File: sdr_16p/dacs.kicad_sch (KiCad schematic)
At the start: 1 part, among them U5 ADAU1962AWBSTZ

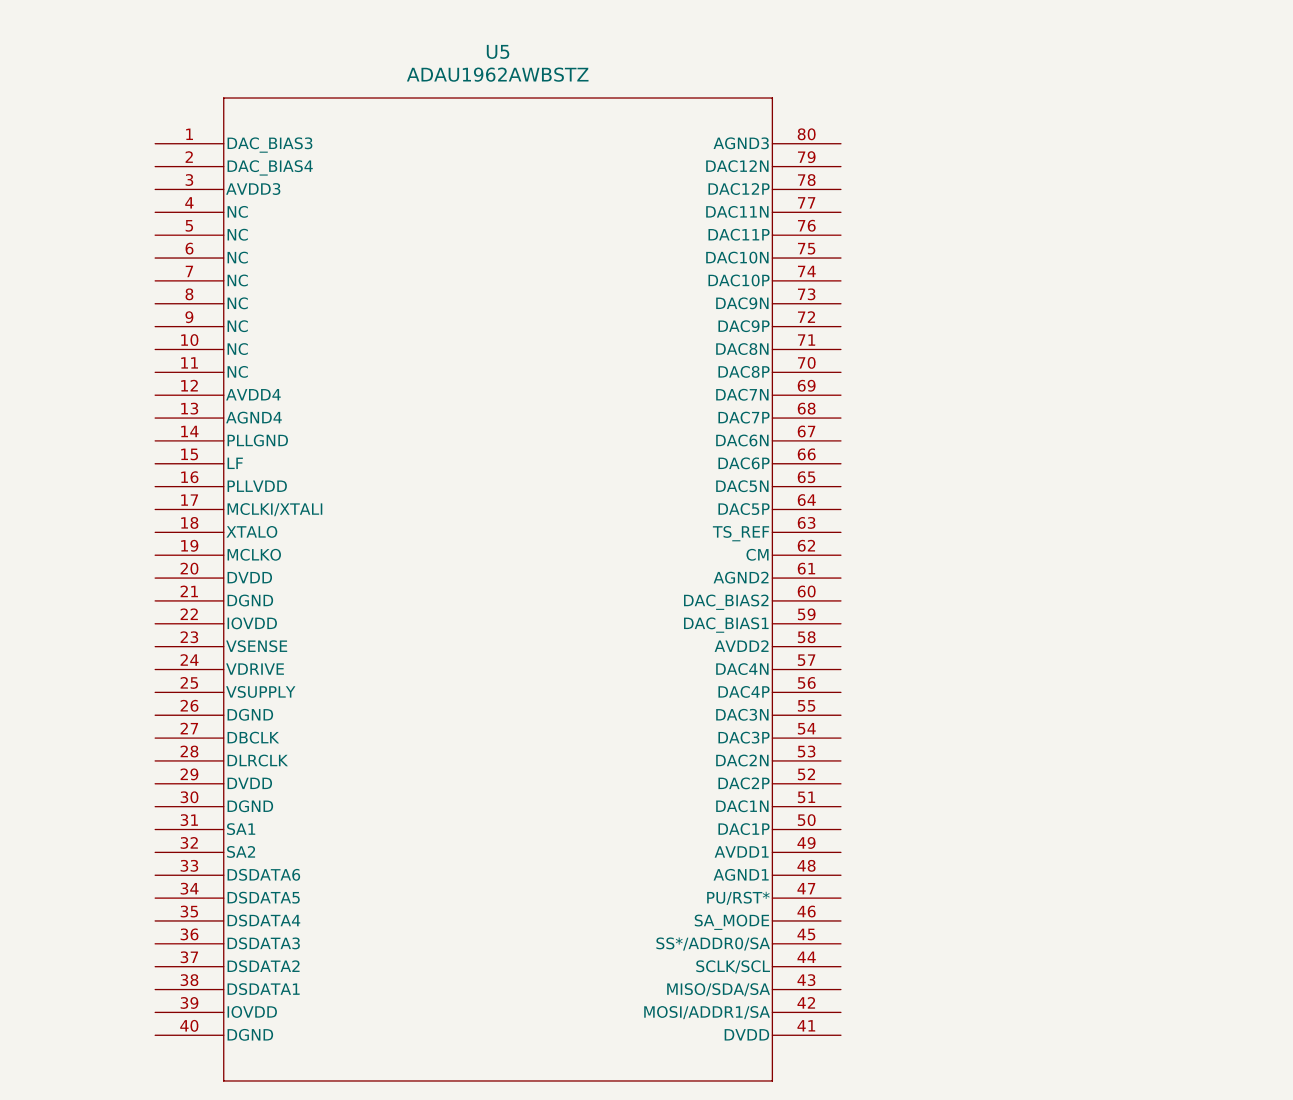
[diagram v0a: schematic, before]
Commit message: updated to 16 channel SE
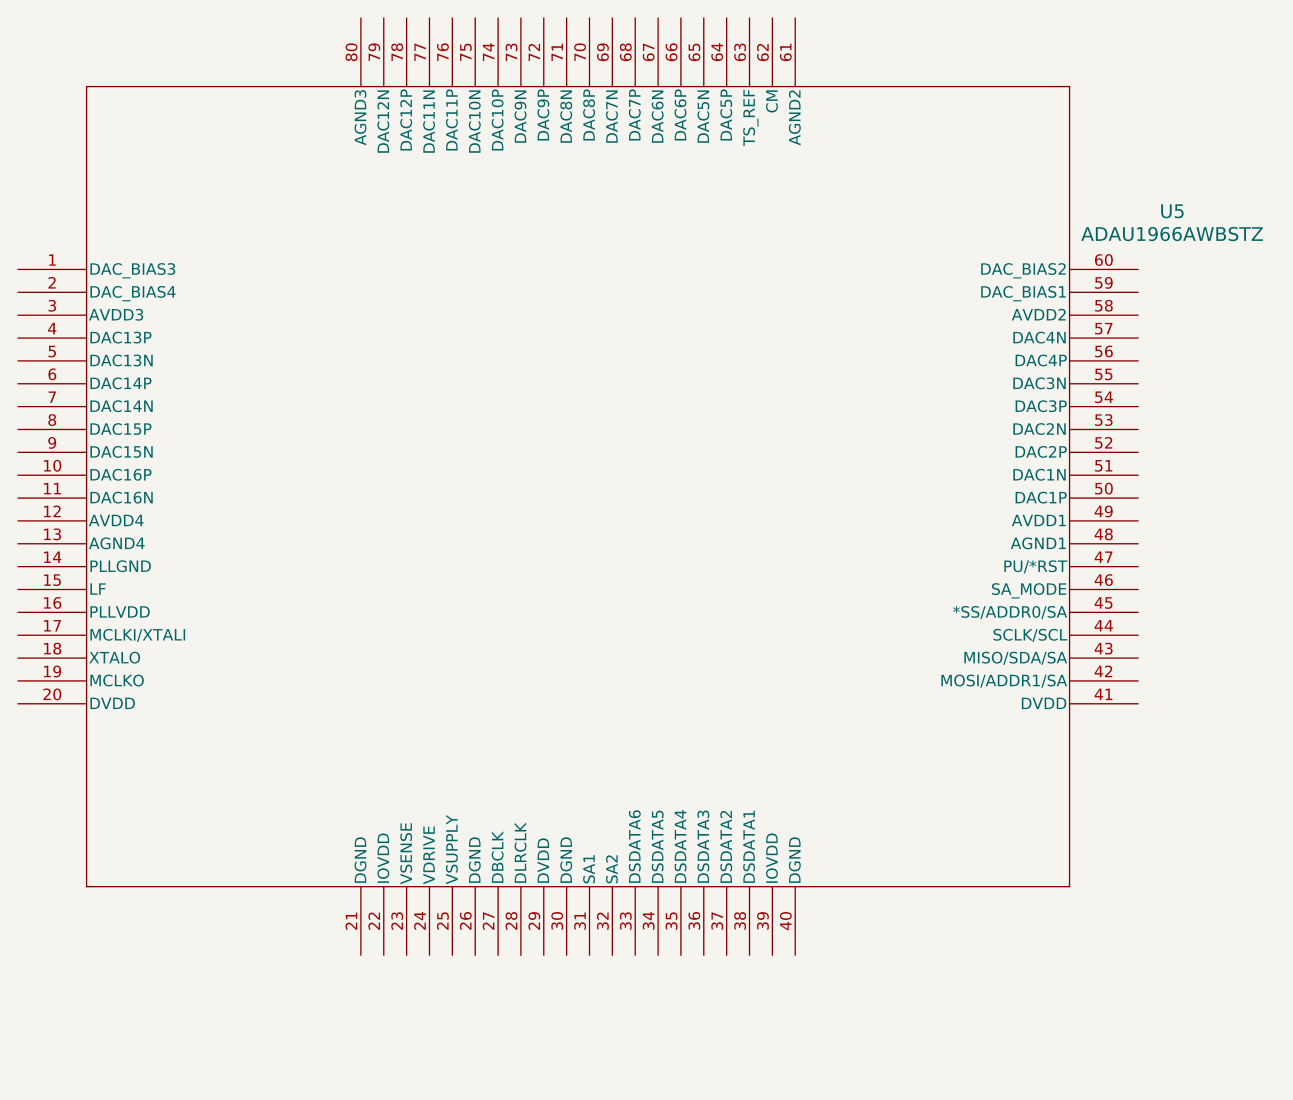
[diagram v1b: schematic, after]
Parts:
- removed U5: ADAU1962AWBSTZ, ST_80_2_ADI, symbol ADAU1962A:ADAU1962AWBSTZ
- added U5: ADAU1966AWBSTZ, ST_80_2_ADI, symbol ADAU1966:ADAU1966AWBSTZ
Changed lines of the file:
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@@
 	)
 	(symbol
-		(lib_id "ADAU1962A:ADAU1962AWBSTZ")
-		(at 171.45 78.74 0)
+		(lib_id "ADAU1966:ADAU1966AWBSTZ")
+		(at 156.21 92.71 0)
 		(unit 1)
 		(exclude_from_sim no)
@@
 		(fields_autoplaced yes)
 		(property "Reference" "U5"
-			(at 209.55 68.58 0)
+			(at 284.48 86.2898 0)
 			(effects
 				(font
@@
 			)
 		)
-		(property "Value" "ADAU1962AWBSTZ"
-			(at 209.55 71.12 0)
+		(property "Value" "ADAU1966AWBSTZ"
+			(at 284.48 88.8298 0)
 			(effects
 				(font
@@
 		)
 		(property "Footprint" "ST_80_2_ADI"
-			(at 171.45 78.74 0)
+			(at 156.21 92.71 0)
 			(effects
 				(font
@@
 			)
 		)
-		(property "Datasheet" "https://www.analog.com/media/en/technical-documentation/data-sheets/ADAU1962A.pdf"
-			(at 171.45 78.74 0)
+		(property "Datasheet" "https://www.analog.com/media/en/technical-documentation/data-sheets/ADAU1966A.pdf"
+			(at 156.21 92.71 0)
 			(effects
 				(font
@@
 		)
 		(property "Description" ""
-			(at 171.45 78.74 0)
+			(at 156.21 92.71 0)
 			(effects
 				(font
@@
 			)
 		)
+		(pin "31"
+		)
+		(pin "57"
+		)
+		(pin "66"
+		)
+		(pin "30"
+		)
+		(pin "71"
+		)
+		(pin "64"
+		)
+		(pin "32"
+		)
+		(pin "68"
+		)
 		(pin "48"
 		)
+		(pin "65"
+		)
+		(pin "58"
+		)
+		(pin "52"
+		)
+		(pin "67"
+		)
+		(pin "36"
+		)
+		(pin "44"
+		)
+		(pin "51"
+		)
+		(pin "45"
+		)
+		(pin "54"
+		)
+		(pin "42"
+		)
+		(pin "35"
+		)
+		(pin "37"
+		)
+		(pin "59"
+		)
+		(pin "40"
+		)
+		(pin "70"
+		)
+		(pin "69"
+		)
+		(pin "34"
+		)
+		(pin "60"
+		)
+		(pin "61"
+		)
+		(pin "41"
+		)
+		(pin "80"
+		)
+		(pin "47"
+		)
+		(pin "27"
+		)
+		(pin "29"
+		)
+		(pin "72"
+		)
+		(pin "77"
+		)
+		(pin "39"
+		)
+		(pin "55"
+		)
+		(pin "56"
+		)
+		(pin "62"
+		)
+		(pin "24"
+		)
+		(pin "10"
+		)
 		(pin "49"
 		)
-		(pin "35"
-		)
-		(pin "27"
-		)
-		(pin "29"
-		)
-		(pin "57"
+		(pin "46"
+		)
+		(pin "15"
+		)
+		(pin "19"
 		)
 		(pin "75"
 		)
+		(pin "79"
+		)
+		(pin "18"
+		)
+		(pin "3"
+		)
+		(pin "6"
+		)
+		(pin "5"
+		)
+		(pin "4"
+		)
+		(pin "2"
+		)
+		(pin "1"
+		)
+		(pin "33"
+		)
 		(pin "76"
 		)
+		(pin "20"
+		)
+		(pin "25"
+		)
+		(pin "12"
+		)
+		(pin "17"
+		)
+		(pin "8"
+		)
+		(pin "22"
+		)
+		(pin "21"
+		)
+		(pin "23"
+		)
 		(pin "74"
 		)
-		(pin "39"
-		)
-		(pin "80"
-		)
-		(pin "64"
-		)
-		(pin "8"
-		)
-		(pin "69"
-		)
-		(pin "45"
-		)
-		(pin "44"
+		(pin "16"
+		)
+		(pin "9"
 		)
 		(pin "43"
 		)
-		(pin "46"
-		)
-		(pin "62"
-		)
-		(pin "23"
-		)
-		(pin "51"
-		)
-		(pin "2"
-		)
-		(pin "5"
-		)
-		(pin "20"
-		)
-		(pin "52"
-		)
-		(pin "36"
-		)
-		(pin "54"
-		)
-		(pin "66"
+		(pin "28"
+		)
+		(pin "14"
+		)
+		(pin "38"
+		)
+		(pin "78"
+		)
+		(pin "73"
+		)
+		(pin "26"
 		)
 		(pin "50"
 		)
+		(pin "7"
+		)
+		(pin "11"
+		)
+		(pin "53"
+		)
 		(pin "63"
 		)
-		(pin "79"
-		)
-		(pin "60"
-		)
-		(pin "37"
-		)
-		(pin "59"
-		)
-		(pin "58"
-		)
-		(pin "61"
-		)
-		(pin "1"
-		)
-		(pin "21"
-		)
-		(pin "78"
-		)
-		(pin "71"
-		)
-		(pin "38"
-		)
 		(pin "13"
 		)
-		(pin "24"
-		)
-		(pin "28"
-		)
-		(pin "70"
-		)
-		(pin "18"
-		)
-		(pin "56"
-		)
-		(pin "73"
-		)
-		(pin "6"
-		)
-		(pin "9"
-		)
-		(pin "33"
-		)
-		(pin "17"
-		)
-		(pin "25"
-		)
-		(pin "22"
-		)
-		(pin "15"
-		)
-		(pin "65"
-		)
-		(pin "7"
-		)
-		(pin "53"
-		)
-		(pin "30"
-		)
-		(pin "32"
-		)
-		(pin "19"
-		)
-		(pin "55"
-		)
-		(pin "77"
-		)
-		(pin "41"
-		)
-		(pin "16"
-		)
-		(pin "42"
-		)
-		(pin "10"
-		)
-		(pin "47"
-		)
-		(pin "26"
-		)
-		(pin "11"
-		)
-		(pin "31"
-		)
-		(pin "14"
-		)
-		(pin "40"
-		)
-		(pin "72"
-		)
-		(pin "68"
-		)
-		(pin "34"
-		)
-		(pin "67"
-		)
-		(pin "4"
-		)
-		(pin "3"
-		)
-		(pin "12"
-		)
 		(instances
-			(project "sdr_12p"
+			(project ""
 				(path "/fe42ca2f-2bb8-4d5a-9e84-807788ed632f/1097e363-2947-4914-97f0-a09e0bb38c3a"
 					(reference "U5")
